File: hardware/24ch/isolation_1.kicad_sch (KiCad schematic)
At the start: 51 parts, among them U401 B0505S-1WR2, U402 LP2985IM5X-3.3, U403 ISO7761DWR, U404 ISO7761DWR, U405 ISO7761DWR, U406 REF3030AIDBZR, U407 MCP6001T-I/OT

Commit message: 24ch cheaper-parts variant (0036): TMP126, CA-IS3761HW, RS-485 DNP, drop-in swaps
- CJ sensors ADT7310 x6 -> TMP126DCKR (C5219998); R443 22k DIN_ISO-DOUT_ISO for the
  3-wire SIO, R415 removed, ALERT grounded. Sensors moved <= 8 mm to clear spots beside
  their 100 nF (no closer spot to the terminals without touching TC traces, 0035 D2).
- ISO7761 -> CA-IS3761HW (same pinout, 5F/1R, default high); BOCHEN 3296W trimmer;
  SAMWHA 22u 1210.
- RS-485 block DNP: footprints kept; fab.py drops DNP parts from BOM/CPL and writes
  DNP.txt; cost.py skips them. External window watchdog tried and removed (owner).
- gen/delta.py: carry a schematic change onto the routed board (replace/add/remove,
  re-net, DNP, OLD>NEW@DEG reuse); it never deletes another net's track under a pad.
- Board: incremental edits only; analog nets (TC*, V_BIAS, VREF, REF*) identical to
  the pre-0036 board. Gates: ERC 0/0 (471 symbols); fab.py DRC/unconnected/parity
  0/0/0; pincaps 0 over. Parts ~$105 -> ~$72/board (CALCULATIONS 8.1, by hand).
- Docs: decision 0036, CALCULATIONS 8, ISSUES (I-109, I-114, I-119, I-104, I-094,
  new I-123 stock), STATE, 24ch README, superseded.txt.

Co-Authored-By: Claude Opus 5.5 <noreply@anthropic.com>
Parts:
- removed R415: 100k, Resistor_SMD:R_0805_2012Metric, symbol Device:R
- added R443: 22k, Resistor_SMD:R_0805_2012Metric, symbol Device:R
- U403, U404, U405: value ISO7761DWR -> CA-IS3761HW; LCSC C2871529 -> C528656; MPN ISO7761DWR -> CA-IS3761HW; Manufacturer TI -> Chipanalog
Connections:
- net DIN_ISO: now also R443.1
- net DOUT_ISO: now also R443.2
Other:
- note added: "Digital isolators: SPI to the three AD7124 and six TMP126"
- note removed: "Digital isolators: SPI to the three AD7124 and six ADT7310"
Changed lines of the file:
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@@
 		)
 	)
-	(text "Digital isolators: SPI to the three AD7124 and six ADT7310"
+	(text "Digital isolators: SPI to the three AD7124 and six TMP126"
 		(exclude_from_sim no)
 		(at 15 67.511 0)
@@
 			)
 		)
-		(property "Value" "ISO7761DWR"
+		(property "Value" "CA-IS3761HW"
 			(at 49.26 90.84 0)
 			(effects
@@
 			)
 		)
-		(property "Description" ""
+		(property "Description" "ISO7761 pinout, 5 forward / 1 reverse, default output high (0036)"
 			(at 38.1 109.22 0)
 			(effects
@@
 			)
 		)
-		(property "MPN" "ISO7761DWR"
+		(property "MPN" "CA-IS3761HW"
 			(at 38.1 109.22 0)
 			(effects
@@
 			)
 		)
-		(property "Manufacturer" "TI"
+		(property "Manufacturer" "Chipanalog"
 			(at 38.1 109.22 0)
 			(effects
@@
 			)
 		)
-		(property "LCSC" "C2871529"
+		(property "LCSC" "C528656"
 			(at 38.1 109.22 0)
 			(effects
@@
 			)
 		)
-		(property "Value" "ISO7761DWR"
+		(property "Value" "CA-IS3761HW"
 			(at 128 90.84 0)
 			(effects
@@
 			)
 		)
-		(property "Description" ""
+		(property "Description" "ISO7761 pinout, 5 forward / 1 reverse, default output high (0036)"
 			(at 116.84 109.22 0)
 			(effects
@@
 			)
 		)
-		(property "MPN" "ISO7761DWR"
+		(property "MPN" "CA-IS3761HW"
 			(at 116.84 109.22 0)
 			(effects
@@
 			)
 		)
-		(property "Manufacturer" "TI"
+		(property "Manufacturer" "Chipanalog"
 			(at 116.84 109.22 0)
 			(effects
@@
 			)
 		)
-		(property "LCSC" "C2871529"
+		(property "LCSC" "C528656"
 			(at 116.84 109.22 0)
 			(effects
@@
 			)
 		)
-		(property "Value" "ISO7761DWR"
+		(property "Value" "CA-IS3761HW"
 			(at 206.74 90.84 0)
 			(effects
@@
 			)
 		)
-		(property "Description" ""
+		(property "Description" "ISO7761 pinout, 5 forward / 1 reverse, default output high (0036)"
 			(at 195.58 109.22 0)
 			(effects
@@
 			)
 		)
-		(property "MPN" "ISO7761DWR"
+		(property "MPN" "CA-IS3761HW"
 			(at 195.58 109.22 0)
 			(effects
@@
 			)
 		)
-		(property "Manufacturer" "TI"
+		(property "Manufacturer" "Chipanalog"
 			(at 195.58 109.22 0)
 			(effects
@@
 			)
 		)
-		(property "LCSC" "C2871529"
+		(property "LCSC" "C528656"
 			(at 195.58 109.22 0)
 			(effects
@@
 		(on_board yes)
 		(dnp no)
-		(property "Reference" "R415"
+		(property "Reference" "R443"
 			(at 65.316 166.64 0)
 			(effects
@@
 			)
 		)
-		(property "Value" "100k"
+		(property "Value" "22k"
 			(at 65.316 169.24 0)
 			(effects
@@
 			)
 		)
-		(property "Description" "defined DOUT with all devices deselected"
+		(property "Description" "TMP126 3-wire SPI: MOSI reaches each SIO through 22k, SIO drives DOUT; 22k not 10k keeps the AD7124 DOUT load ~0.15 mA (spec at 0.1 mA); also defines DOUT when all are deselected (0036)"
 			(at 63.5 167.64 0)
 			(effects
@@
 			)
 		)
-		(property "MPN" "0805W8F1003T5E"
+		(property "MPN" "0805W8F2202T5E"
 			(at 63.5 167.64 0)
 			(effects
@@
 			)
 		)
-		(property "LCSC" "C149504"
+		(property "LCSC" "C17560"
 			(at 63.5 167.64 0)
 			(effects
@@
 			(project "thermo24"
 				(path "/396a983b-08a5-57c9-b07a-3d6ae939cc55/4bce2767-831f-5e10-a27a-e3e09fc61d98"
-					(reference "R415")
+					(reference "R443")
 					(unit 1)
 				)
@@
 		)
 	)
-	(global_label "DOUT_ISO"
+	(global_label "DIN_ISO"
 		(shape bidirectional)
 		(at 63.5 161.29 90)
@@
 		)
 	)
-	(global_label "+3V3_ISO"
+	(global_label "DOUT_ISO"
 		(shape bidirectional)
 		(at 63.5 173.99 270)

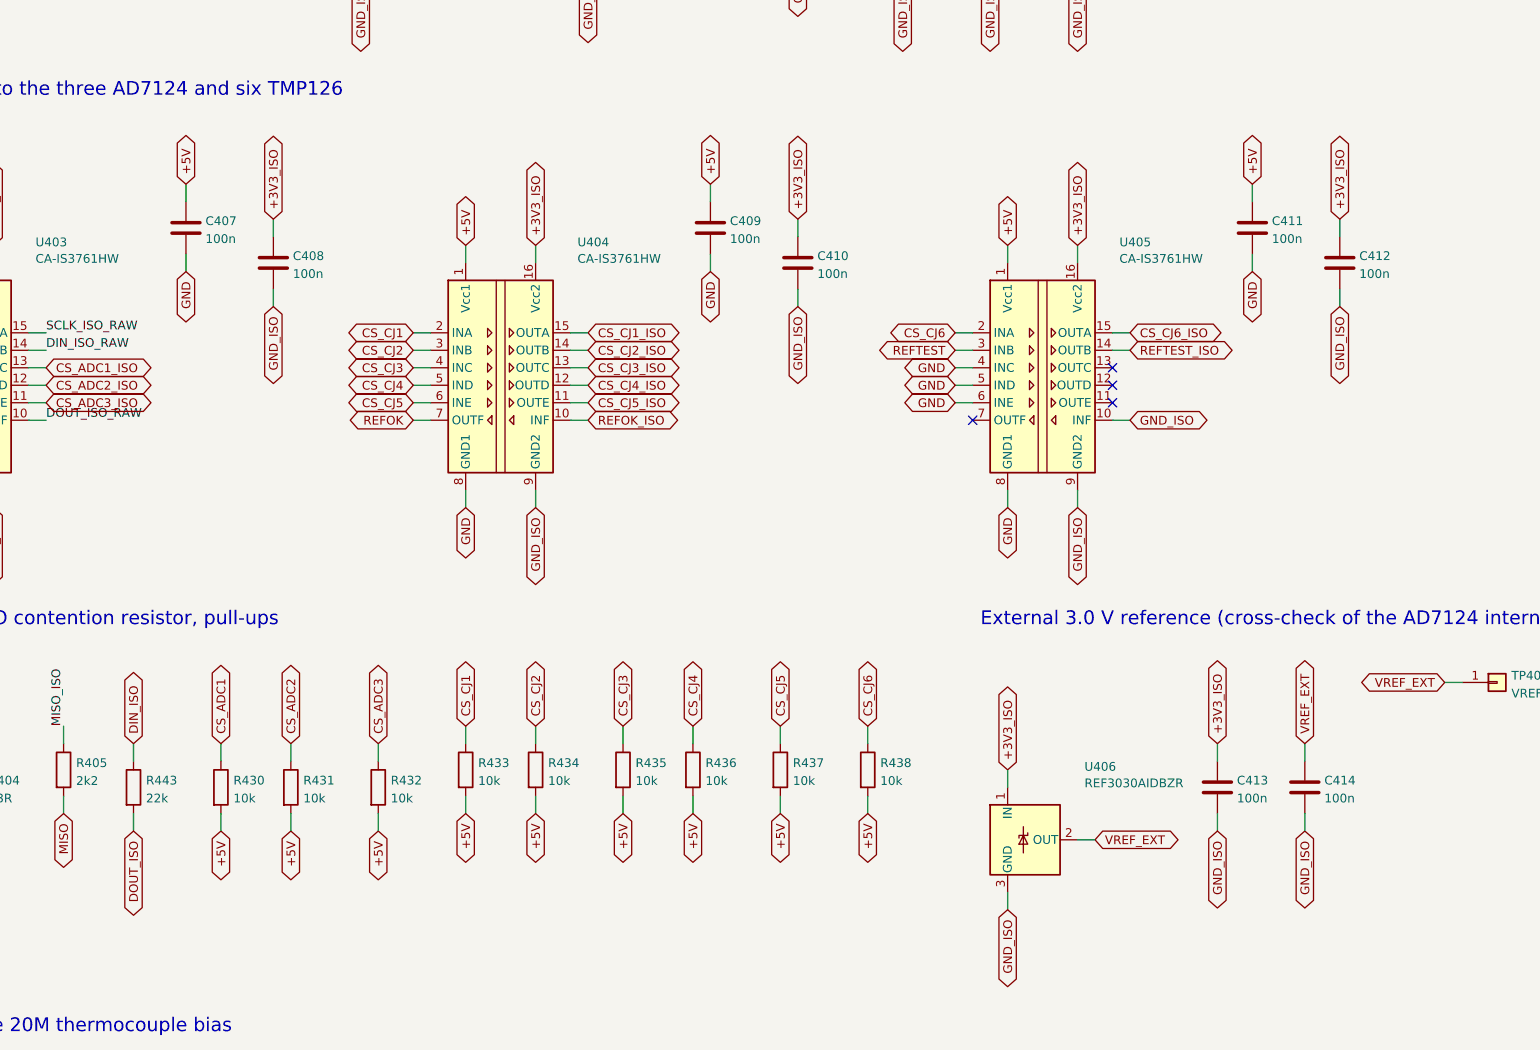
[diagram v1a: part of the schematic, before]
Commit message: 24ch REV A4 (WIP): gated TMP126 SIO driver, PD5 = SIO_WR_N, ESC via diodes
- PD5 (was BTN_ESC) drives SIO_WR_N through spare U405 channel C to U411
  74LVC1G125 (OE); DIN -> U411 -> R446 220R -> DOUT_ISO; R445 10k, R447 100k,
  C421 100n, R439 10k pull-up. R443 22k removed (R446 reuses its footprint).
  Same circuit as hardware/family (fixes the TMP126 SIO edge, 1.2-1.6 us vs 100 ns).
- ESC button kept: D501/D502 1N4148W pull BTN_UP and BTN_DOWN together;
  firmware reads UP+DOWN as ESC.
- Board edited incrementally (delta.py, capnear.py, maze.py with In2 for
  SIO_DRV / SIO_WR_N_ISO); dead DIN branch to the old R443 pad removed.
- Gates: build.py ERC 0 errors 0 warnings, netlist 0 mismatches;
  finish.py DRC (errors, refilled) 0 violations, 0 unconnected; pincaps 0 over
  (U411 added). Silk, full DRC, fab release still to do.
- Title/release names REV A4.

Co-Authored-By: Claude Opus 5.5 <noreply@anthropic.com>
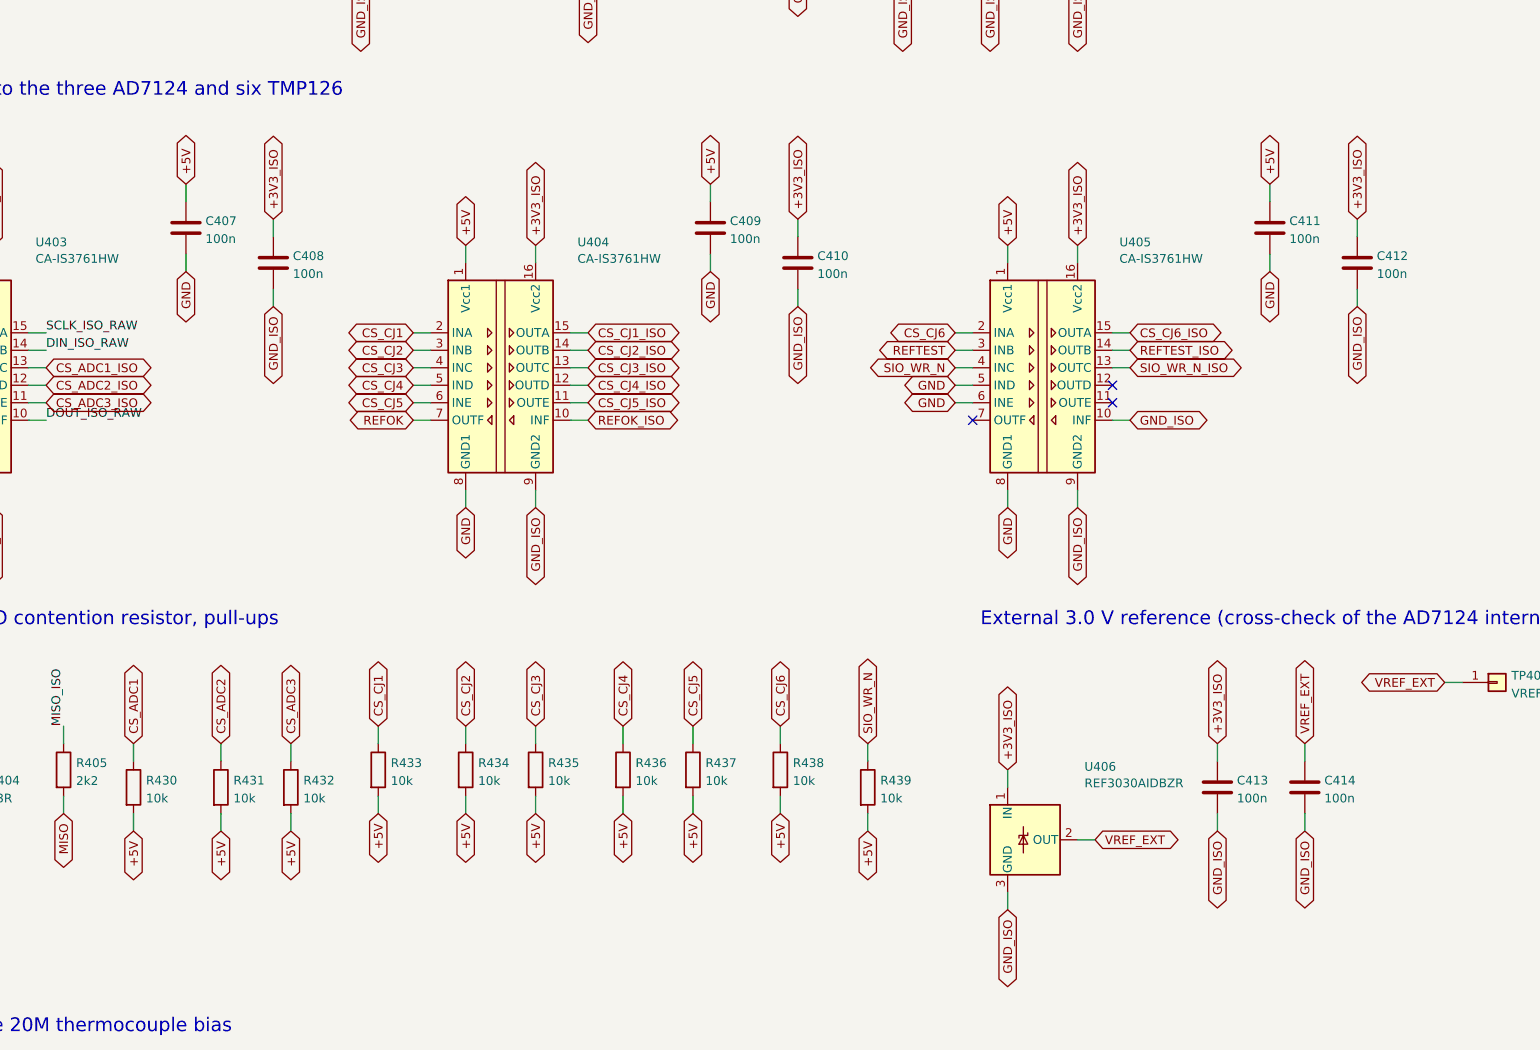
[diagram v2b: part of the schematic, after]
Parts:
- removed R443: 22k, Resistor_SMD:R_0805_2012Metric, symbol Device:R
- added R439: 10k, Resistor_SMD:R_0805_2012Metric, symbol Device:R
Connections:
- net +5V: now also R439.2
- net GND: no longer U405.4 (INC)
- net SIO_WR_N_ISO: now reaches U405.13 (OUTC)
- new net SIO_WR_N: R439.1, U405.4 (INC)
- no-connect marks 4 -> 3
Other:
- moved on the sheet: C411, C412, R430, R431, R432, R433, R434, R435, R436, R437, R438
